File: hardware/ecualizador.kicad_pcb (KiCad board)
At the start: 2 copper layers, 200 x 120 mm, 80 parts, among them J1 Entrada de línea 3,5 mm, J2 Salida de línea 3,5 mm, J3 PAM8403, J4 TFT ILI9341 2,8" SPI, SW1 Pulsador, U1 MCP6004, U2 MCP6004, U3 MCP6004, U4 MCP6004, U5 ESP32-DevKitC V4

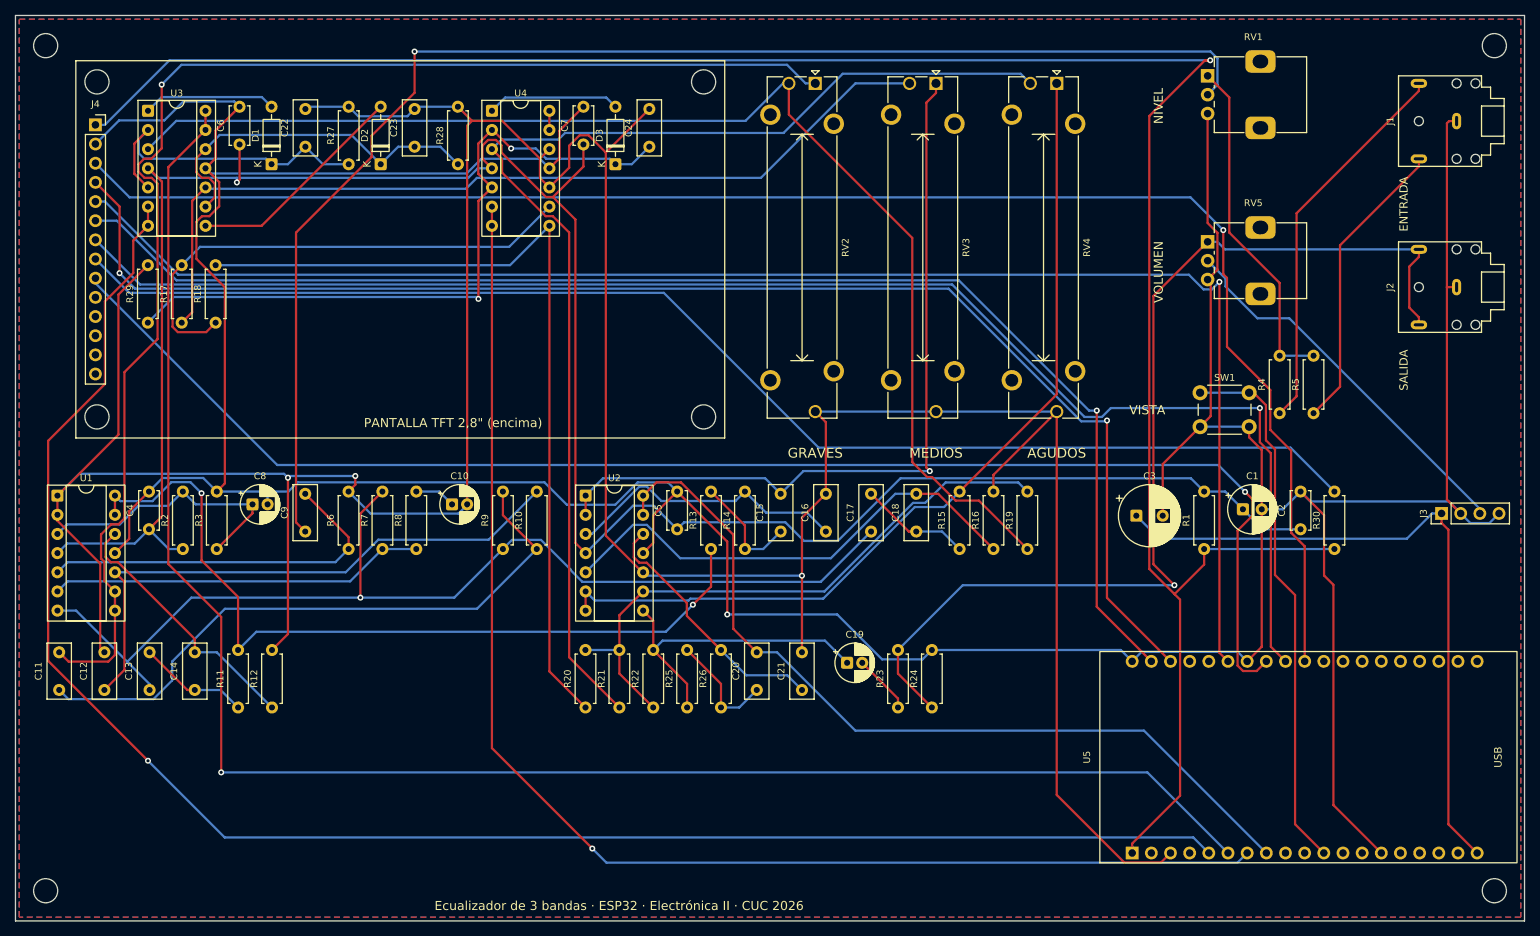
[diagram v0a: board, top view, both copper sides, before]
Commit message: Completa PCB de una cara, documentación LaTeX y demo con audio sincronizado
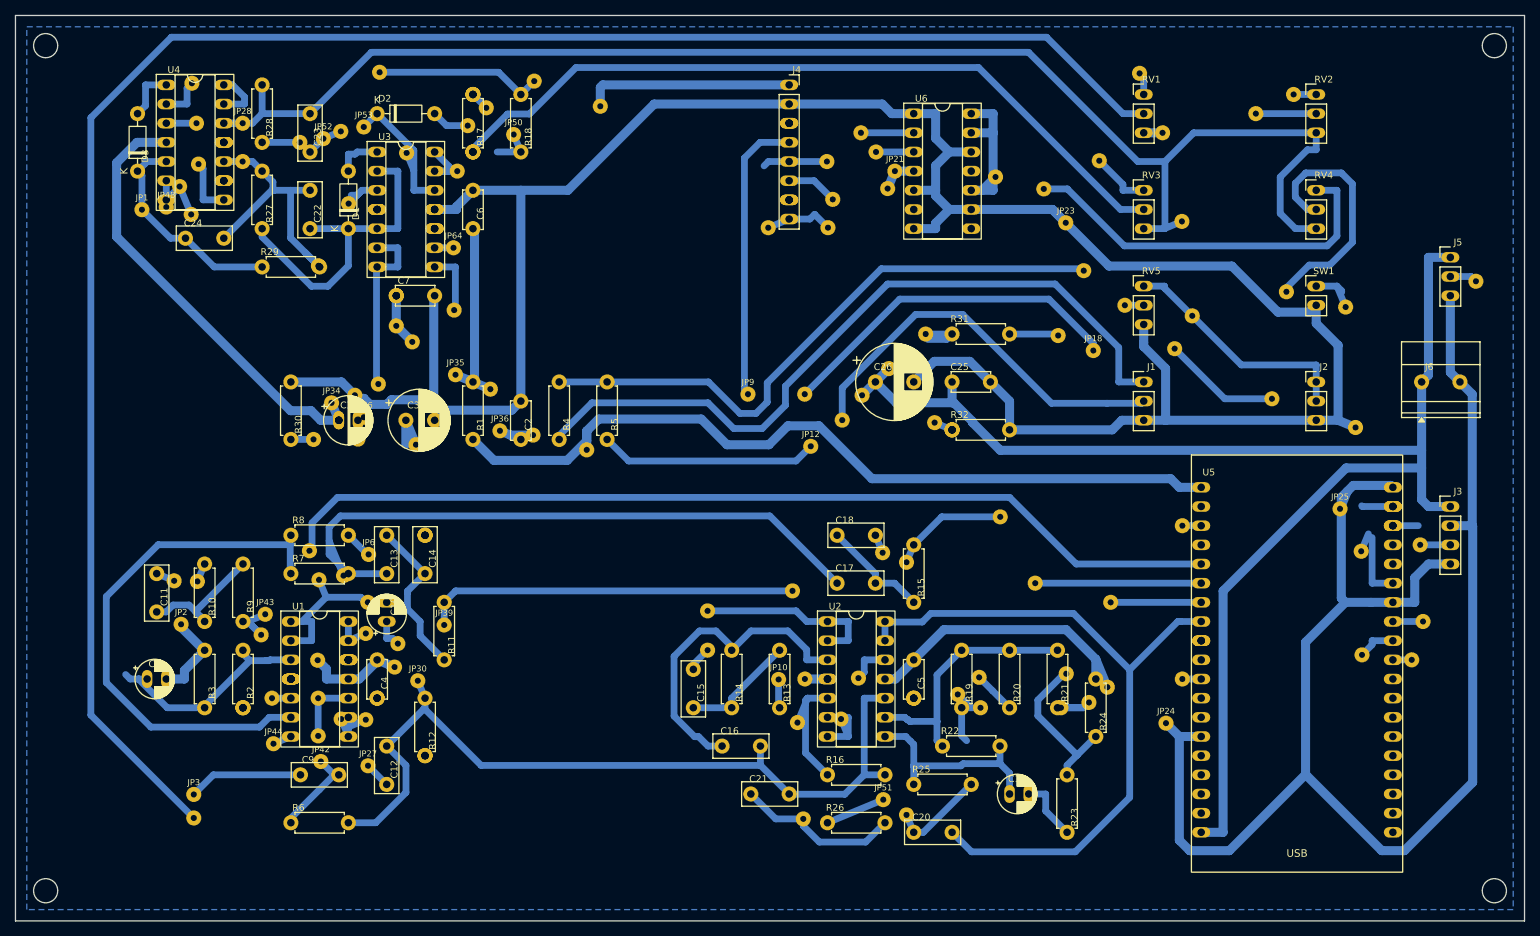
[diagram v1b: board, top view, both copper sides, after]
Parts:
- removed H5, H6, H7, H8: MountingHole_3.2mm_M3, MountingHole:MountingHole_3.2mm_M3
- added C25: 100n, Ecualizador:UnaCara_C25, F.Cu at (124.1, 48.6)
- added C26: 1000u 10V, Ecualizador:UnaCara_C26, F.Cu at (114.0, 48.6)
- added J5: NeoPixel 5V DIN GND, Ecualizador:UnaCara_J5, F.Cu at (190.2, 32.1)
- added J6: Entrada 5V 3A, Ecualizador:UnaCara_J6, F.Cu at (186.4, 48.6)
- added JP1, JP10, JP11, JP12, JP13, JP14, JP15, JP16, JP17, JP18, JP19, JP2, JP20, JP21, JP22, JP23, JP24, JP25, JP26, JP27, JP28, JP29, JP3, JP30, JP31, JP32, JP33, JP34, JP35, JP36, JP37, JP38, JP39, JP4, JP40, JP41, JP42, JP43, JP44, JP45, JP46, JP47, JP48, JP49, JP5, JP50, JP51, JP52, JP53, JP54, JP55, JP56, JP57, JP58, JP59, JP6, JP60, JP61, JP62, JP63, JP64, JP65, JP66, JP7, JP8, JP9: Puente aislado, , F.Cu at (0.00, 0.00)
- added JP67, JP68, JP69, JP70, JP71, JP72, JP73, JP74, JP75, JP76, JP77, JP78, JP79: Puente a terminal, , F.Cu at (0.00, 0.00)
- added R31: 330, Ecualizador:UnaCara_R31, F.Cu at (124.1, 42.2)
- added R32: 10k, Ecualizador:UnaCara_R32, F.Cu at (124.1, 54.9)
- added U6: 74AHCT125, Ecualizador:UnaCara_U6, F.Cu at (119.0, 13.0)
- C1: footprint Capacitor_THT:CP_Radial_D6.3mm_P2.50mm -> Ecualizador:UnaCara_C1
- C10: footprint Capacitor_THT:CP_Radial_D5.0mm_P2.00mm -> Ecualizador:UnaCara_C10
- C11: footprint Capacitor_THT:C_Rect_L7.2mm_W3.0mm_P5.00mm_FKS2_FKP2_MKS2_MKP2 -> Ecualizador:UnaCara_C11
- C12: footprint Capacitor_THT:C_Rect_L7.2mm_W3.0mm_P5.00mm_FKS2_FKP2_MKS2_MKP2 -> Ecualizador:UnaCara_C12
- C13: footprint Capacitor_THT:C_Rect_L7.2mm_W3.0mm_P5.00mm_FKS2_FKP2_MKS2_MKP2 -> Ecualizador:UnaCara_C13
- C14: footprint Capacitor_THT:C_Rect_L7.2mm_W3.0mm_P5.00mm_FKS2_FKP2_MKS2_MKP2 -> Ecualizador:UnaCara_C14
- C15: footprint Capacitor_THT:C_Rect_L7.2mm_W3.0mm_P5.00mm_FKS2_FKP2_MKS2_MKP2 -> Ecualizador:UnaCara_C15
- C16: footprint Capacitor_THT:C_Rect_L7.2mm_W3.0mm_P5.00mm_FKS2_FKP2_MKS2_MKP2 -> Ecualizador:UnaCara_C16
- C17: footprint Capacitor_THT:C_Rect_L7.2mm_W3.0mm_P5.00mm_FKS2_FKP2_MKS2_MKP2 -> Ecualizador:UnaCara_C17
- C18: footprint Capacitor_THT:C_Rect_L7.2mm_W3.0mm_P5.00mm_FKS2_FKP2_MKS2_MKP2 -> Ecualizador:UnaCara_C18
- C19: footprint Capacitor_THT:CP_Radial_D5.0mm_P2.00mm -> Ecualizador:UnaCara_C19
- C2: footprint Capacitor_THT:C_Disc_D5.0mm_W2.5mm_P5.00mm -> Ecualizador:UnaCara_C2
- C20: footprint Capacitor_THT:C_Rect_L7.2mm_W3.0mm_P5.00mm_FKS2_FKP2_MKS2_MKP2 -> Ecualizador:UnaCara_C20
- C21: footprint Capacitor_THT:C_Rect_L7.2mm_W3.0mm_P5.00mm_FKS2_FKP2_MKS2_MKP2 -> Ecualizador:UnaCara_C21
- C22: footprint Capacitor_THT:C_Rect_L7.2mm_W3.0mm_P5.00mm_FKS2_FKP2_MKS2_MKP2 -> Ecualizador:UnaCara_C22
- C23: footprint Capacitor_THT:C_Rect_L7.2mm_W3.0mm_P5.00mm_FKS2_FKP2_MKS2_MKP2 -> Ecualizador:UnaCara_C23
- C24: footprint Capacitor_THT:C_Rect_L7.2mm_W3.0mm_P5.00mm_FKS2_FKP2_MKS2_MKP2 -> Ecualizador:UnaCara_C24
- C3: footprint Capacitor_THT:CP_Radial_D8.0mm_P3.50mm -> Ecualizador:UnaCara_C3
- C4: footprint Capacitor_THT:C_Disc_D5.0mm_W2.5mm_P5.00mm -> Ecualizador:UnaCara_C4
- C5: footprint Capacitor_THT:C_Disc_D5.0mm_W2.5mm_P5.00mm -> Ecualizador:UnaCara_C5
- C6: footprint Capacitor_THT:C_Disc_D5.0mm_W2.5mm_P5.00mm -> Ecualizador:UnaCara_C6
- C7: footprint Capacitor_THT:C_Disc_D5.0mm_W2.5mm_P5.00mm -> Ecualizador:UnaCara_C7
- C8: footprint Capacitor_THT:CP_Radial_D5.0mm_P2.00mm -> Ecualizador:UnaCara_C8
- C9: footprint Capacitor_THT:C_Rect_L7.2mm_W3.0mm_P5.00mm_FKS2_FKP2_MKS2_MKP2 -> Ecualizador:UnaCara_C9
- D1: footprint Diode_THT:D_DO-35_SOD27_P7.62mm_Horizontal -> Ecualizador:UnaCara_D1
- D2: footprint Diode_THT:D_DO-35_SOD27_P7.62mm_Horizontal -> Ecualizador:UnaCara_D2
- D3: footprint Diode_THT:D_DO-35_SOD27_P7.62mm_Horizontal -> Ecualizador:UnaCara_D3
- J1: footprint Connector_Audio:Jack_3.5mm_CUI_SJ1-3523N_Horizontal -> Ecualizador:UnaCara_J1
- J2: footprint Connector_Audio:Jack_3.5mm_CUI_SJ1-3523N_Horizontal -> Ecualizador:UnaCara_J2
- J3: footprint Connector_PinHeader_2.54mm:PinHeader_1x04_P2.54mm_Vertical -> Ecualizador:UnaCara_J3
- J4: value TFT ILI9341 2,8" SPI -> Waveshare 1.9 ST7789V2; footprint Connector_PinSocket_2.54mm:PinSocket_1x14_P2.54mm_Vertical -> Ecualizador:UnaCara_J4
- R1: footprint Resistor_THT:R_Axial_DIN0207_L6.3mm_D2.5mm_P7.62mm_Horizontal -> Ecualizador:UnaCara_R1
- R10: footprint Resistor_THT:R_Axial_DIN0207_L6.3mm_D2.5mm_P7.62mm_Horizontal -> Ecualizador:UnaCara_R10
- R11: footprint Resistor_THT:R_Axial_DIN0207_L6.3mm_D2.5mm_P7.62mm_Horizontal -> Ecualizador:UnaCara_R11
- R12: footprint Resistor_THT:R_Axial_DIN0207_L6.3mm_D2.5mm_P7.62mm_Horizontal -> Ecualizador:UnaCara_R12
- R13: footprint Resistor_THT:R_Axial_DIN0207_L6.3mm_D2.5mm_P7.62mm_Horizontal -> Ecualizador:UnaCara_R13
- R14: footprint Resistor_THT:R_Axial_DIN0207_L6.3mm_D2.5mm_P7.62mm_Horizontal -> Ecualizador:UnaCara_R14
- R15: footprint Resistor_THT:R_Axial_DIN0207_L6.3mm_D2.5mm_P7.62mm_Horizontal -> Ecualizador:UnaCara_R15
- R16: footprint Resistor_THT:R_Axial_DIN0207_L6.3mm_D2.5mm_P7.62mm_Horizontal -> Ecualizador:UnaCara_R16
- R17: footprint Resistor_THT:R_Axial_DIN0207_L6.3mm_D2.5mm_P7.62mm_Horizontal -> Ecualizador:UnaCara_R17
- R18: footprint Resistor_THT:R_Axial_DIN0207_L6.3mm_D2.5mm_P7.62mm_Horizontal -> Ecualizador:UnaCara_R18
- R19: footprint Resistor_THT:R_Axial_DIN0207_L6.3mm_D2.5mm_P7.62mm_Horizontal -> Ecualizador:UnaCara_R19
- R2: footprint Resistor_THT:R_Axial_DIN0207_L6.3mm_D2.5mm_P7.62mm_Horizontal -> Ecualizador:UnaCara_R2
- R20: footprint Resistor_THT:R_Axial_DIN0207_L6.3mm_D2.5mm_P7.62mm_Horizontal -> Ecualizador:UnaCara_R20
- R21: footprint Resistor_THT:R_Axial_DIN0207_L6.3mm_D2.5mm_P7.62mm_Horizontal -> Ecualizador:UnaCara_R21
- R22: footprint Resistor_THT:R_Axial_DIN0207_L6.3mm_D2.5mm_P7.62mm_Horizontal -> Ecualizador:UnaCara_R22
- R23: footprint Resistor_THT:R_Axial_DIN0207_L6.3mm_D2.5mm_P7.62mm_Horizontal -> Ecualizador:UnaCara_R23
- R24: footprint Resistor_THT:R_Axial_DIN0207_L6.3mm_D2.5mm_P7.62mm_Horizontal -> Ecualizador:UnaCara_R24
- R25: footprint Resistor_THT:R_Axial_DIN0207_L6.3mm_D2.5mm_P7.62mm_Horizontal -> Ecualizador:UnaCara_R25
- R26: footprint Resistor_THT:R_Axial_DIN0207_L6.3mm_D2.5mm_P7.62mm_Horizontal -> Ecualizador:UnaCara_R26
- R27: footprint Resistor_THT:R_Axial_DIN0207_L6.3mm_D2.5mm_P7.62mm_Horizontal -> Ecualizador:UnaCara_R27
- R28: footprint Resistor_THT:R_Axial_DIN0207_L6.3mm_D2.5mm_P7.62mm_Horizontal -> Ecualizador:UnaCara_R28
- R29: footprint Resistor_THT:R_Axial_DIN0207_L6.3mm_D2.5mm_P7.62mm_Horizontal -> Ecualizador:UnaCara_R29
- R3: footprint Resistor_THT:R_Axial_DIN0207_L6.3mm_D2.5mm_P7.62mm_Horizontal -> Ecualizador:UnaCara_R3
- R30: value 10 -> 10k; footprint Resistor_THT:R_Axial_DIN0207_L6.3mm_D2.5mm_P7.62mm_Horizontal -> Ecualizador:UnaCara_R30
- R4: footprint Resistor_THT:R_Axial_DIN0207_L6.3mm_D2.5mm_P7.62mm_Horizontal -> Ecualizador:UnaCara_R4
- R5: footprint Resistor_THT:R_Axial_DIN0207_L6.3mm_D2.5mm_P7.62mm_Horizontal -> Ecualizador:UnaCara_R5
- R6: footprint Resistor_THT:R_Axial_DIN0207_L6.3mm_D2.5mm_P7.62mm_Horizontal -> Ecualizador:UnaCara_R6
- R7: footprint Resistor_THT:R_Axial_DIN0207_L6.3mm_D2.5mm_P7.62mm_Horizontal -> Ecualizador:UnaCara_R7
- R8: footprint Resistor_THT:R_Axial_DIN0207_L6.3mm_D2.5mm_P7.62mm_Horizontal -> Ecualizador:UnaCara_R8
- R9: footprint Resistor_THT:R_Axial_DIN0207_L6.3mm_D2.5mm_P7.62mm_Horizontal -> Ecualizador:UnaCara_R9
- RV1: footprint Potentiometer_THT:Potentiometer_Alps_RK09K_Single_Vertical -> Ecualizador:UnaCara_RV1
- RV2: footprint Potentiometer_THT:Potentiometer_Bourns_PTA3043_Single_Slide -> Ecualizador:UnaCara_RV2
- RV3: footprint Potentiometer_THT:Potentiometer_Bourns_PTA3043_Single_Slide -> Ecualizador:UnaCara_RV3
- RV4: footprint Potentiometer_THT:Potentiometer_Bourns_PTA3043_Single_Slide -> Ecualizador:UnaCara_RV4
- RV5: footprint Potentiometer_THT:Potentiometer_Alps_RK09K_Single_Vertical -> Ecualizador:UnaCara_RV5
- SW1: footprint Button_Switch_THT:SW_PUSH_6mm_H5mm -> Ecualizador:UnaCara_SW1
- U1: footprint Package_DIP:DIP-14_W7.62mm_Socket -> Ecualizador:UnaCara_U1
- U2: footprint Package_DIP:DIP-14_W7.62mm_Socket -> Ecualizador:UnaCara_U2
- U3: footprint Package_DIP:DIP-14_W7.62mm_Socket -> Ecualizador:UnaCara_U3
- U4: footprint Package_DIP:DIP-14_W7.62mm_Socket -> Ecualizador:UnaCara_U4
- U5: footprint Ecualizador:ESP32-DevKitC-38_Zocalo -> Ecualizador:UnaCara_U5
- moved R30 139.1 mm to (36.5, 56.2)
- moved C1 120.4 mm to (42.8, 53.6)
- moved C2 104.0 mm to (67.0, 56.2)
- moved R1 98.0 mm to (60.6, 56.2)
- moved C3 97.6 mm to (51.7, 53.6)
- moved R4 95.5 mm to (72.1, 56.2)
- moved R5 93.7 mm to (78.4, 56.2)
- moved J4 92.1 mm to (102.5, 9.20)
- moved RV2 66.4 mm to (172.4, 10.5), turned to 0 degrees
- moved D3 63.3 mm to (16.2, 20.6)
- moved C24 62.7 mm to (22.5, 29.5), turned to 0 degrees
- moved R21 58.1 mm to (138.1, 91.8)
- moved R20 56.2 mm to (131.8, 91.8)
- moved J1 54.0 mm to (149.5, 48.6), turned to 0 degrees
- moved U5 49.3 mm to (157.1, 62.5), turned to 0 degrees
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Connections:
- J4 pad 3: /TFT_CS -> /TFT_MOSI
- J4 pad 4: /TFT_RST -> /TFT_SCK
- J4 pad 5: /TFT_DC -> /TFT_CS
- J4 pad 6: /TFT_MOSI -> /TFT_DC
- J4 pad 7: /TFT_SCK -> /TFT_RST
- J4 pad 8: /TFT_LED -> /TFT_BL
- R30 pad 1: +3V3 -> /TFT_BL
- R30 pad 2: /TFT_LED -> GND
- U5 pad 27: /TFT_MISO -> /TFT_BL
- U5 pad 9: unconnected-(U5-IO25-Pad9) -> /LED_DATA
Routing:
- net /TFT_CS: track 214.8 -> 11.1 mm, vias 1 -> 0
- net +3.3VA: track 301.6 -> 101.0 mm, vias 1 -> 0
- net /ADC_M: track 230.5 -> 30.3 mm, vias 1 -> 0
- net /TFT_MISO: track 193.4 -> 0.00 mm, vias 1 -> 0
- net /TFT_DC: track 205.0 -> 18.1 mm, vias 1 -> 0
- net /TFT_RST: track 188.1 -> 3.37 mm, vias 2 -> 0
- net /TFT_LED: track 177.0 -> 0.00 mm
- net /TFT_MOSI: track 179.4 -> 4.17 mm, vias 1 -> 0
- net /GRAVES: track 180.5 -> 13.0 mm, vias 1 -> 0
- net /ADC_A: track 178.7 -> 22.0 mm, vias 1 -> 0
- net +3V3: track 290.7 -> 136.7 mm, vias 1 -> 0
- net /G_W: track 165.5 -> 23.8 mm
- net +5V: track 90.1 -> 224.6 mm
- net /A_W: track 157.6 -> 45.0 mm
- net /VREF: track 485.8 -> 373.3 mm, vias 3 -> 0
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- removed copper zone on F.Cu, net GND
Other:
- board text removed: "AGUDOS"
- board text removed: "ENTRADA"
- board text removed: "Ecualizador de 3 bandas · ESP32 · Electrónica II · CUC 2026"
- board text removed: "GRAVES"
- board text removed: "MEDIOS"
- board text removed: "NIVEL"
- board text removed: "PANTALLA TFT 2,8" (encima)"
- board text removed: "SALIDA"
- board text removed: "VISTA"
- board text removed: "VOLUMEN"
